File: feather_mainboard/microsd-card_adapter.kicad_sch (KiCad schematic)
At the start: 13 parts, among them J4 693071020811, J5 61300211121, J7 61300211121, J8 61300211121

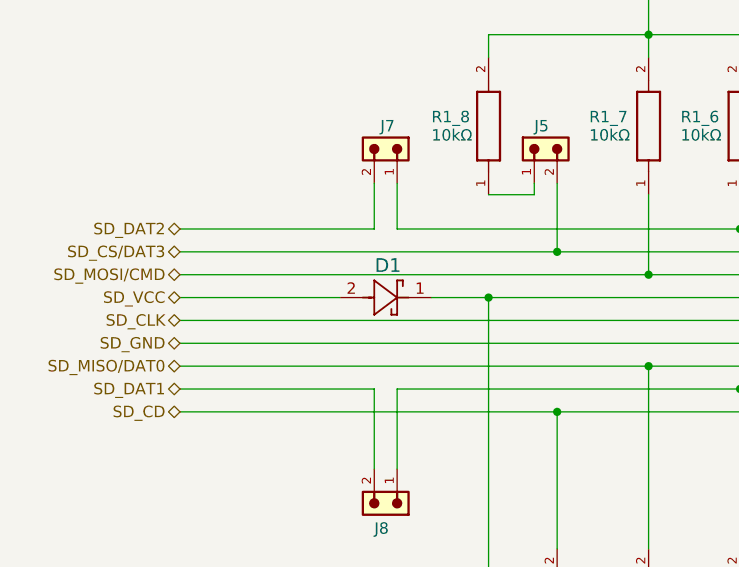
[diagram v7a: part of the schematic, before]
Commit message: Removed the diode, since it is not needed
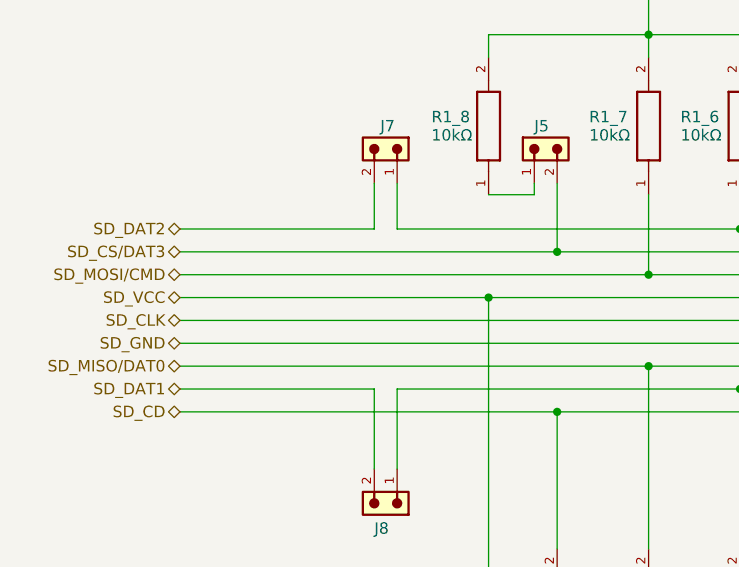
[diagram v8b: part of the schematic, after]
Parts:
- removed D1: PMEG6010CEH_115, Custom footprints:SDO_SOD123F_NEX, symbol SDO_SOD123F_NEX:PMEG6010CEH_115
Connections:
- net SD_VCC: now also C1_4.2, C2_2.2, J4.4 (VDD), R1_10.1, R1_11.1, R1_6.2, R1_7.2, R1_8.2, R1_9.1
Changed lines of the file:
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@@
-	(wire
-		(pts
-			(xy 120.65 99.06) (xy 127 99.06)
-		)
-		(stroke
-			(width 0)
-			(type default)
-		)
-	)
 	(wire
 		(pts
@@
 	(wire
 		(pts
-			(xy 92.71 99.06) (xy 110.49 99.06)
+			(xy 92.71 99.06) (xy 127 99.06)
 		)
 		(stroke
@@
 		(shape bidirectional)
 		(at 92.71 106.68 180)
-		(fields_autoplaced yes)
 		(effects
 			(font
@@
 		(shape bidirectional)
 		(at 92.71 109.22 180)
-		(fields_autoplaced yes)
 		(effects
 			(font
@@
 		(shape bidirectional)
 		(at 92.71 104.14 180)
-		(fields_autoplaced yes)
 		(effects
 			(font
@@
 		(shape bidirectional)
 		(at 92.71 91.44 180)
-		(fields_autoplaced yes)
 		(effects
 			(font
@@
 		(shape bidirectional)
 		(at 92.71 93.98 180)
-		(fields_autoplaced yes)
 		(effects
 			(font
@@
 		(shape bidirectional)
 		(at 92.71 111.76 180)
-		(fields_autoplaced yes)
 		(effects
 			(font
@@
 		(shape bidirectional)
 		(at 92.71 99.06 180)
-		(fields_autoplaced yes)
 		(effects
 			(font
@@
 		(shape bidirectional)
 		(at 92.71 101.6 180)
-		(fields_autoplaced yes)
 		(effects
 			(font
@@
 		(shape bidirectional)
 		(at 92.71 96.52 180)
-		(fields_autoplaced yes)
 		(effects
 			(font
@@
 					(unit 1)
 				)
-			)
-		)
-	)
-	(symbol
-		(lib_id "SDO_SOD123F_NEX:PMEG6010CEH_115")
-		(at 110.49 99.06 0)
-		(unit 1)
-		(exclude_from_sim no)
-		(in_bom yes)
-		(on_board yes)
-		(dnp no)
-		(property "Reference" "D1"
-			(at 115.824 95.504 0)
-			(effects
-				(font
-					(size 1.524 1.524)
-				)
-			)
-		)
-		(property "Value" "PMEG6010CEH_115"
-			(at 115.57 95.25 0)
-			(effects
-				(font
-					(size 1.524 1.524)
-				)
-				(hide yes)
-			)
-		)
-		(property "Footprint" "Custom footprints:SDO_SOD123F_NEX"
-			(at 110.49 99.06 0)
-			(effects
-				(font
-					(size 1.27 1.27)
-					(italic yes)
-				)
-				(hide yes)
-			)
-		)
-		(property "Datasheet" "PMEG6010CEH_115"
-			(at 110.49 99.06 0)
-			(effects
-				(font
-					(size 1.27 1.27)
-					(italic yes)
-				)
-				(hide yes)
-			)
-		)
-		(property "Description" ""
-			(at 110.49 99.06 0)
-			(effects
-				(font
-					(size 1.27 1.27)
-				)
-				(hide yes)
-			)
-		)
-		(pin "2"
-		)
-		(pin "1"
-		)
-		(instances
-			(project "feather_mainboard"
-				(path "/e1e12730-ab4f-45db-8b66-c1e0f78e2f00/6bb461df-e058-49ab-990d-543fb2df67dd"
-					(reference "D1")
-					(unit 1)
-				)
